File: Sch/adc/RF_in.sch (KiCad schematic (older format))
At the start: 48 parts, among them J3 JP2, J4 JP2, U1 LTC2292, U2 BGA2818, U3 TLV711, X1 ECS-TXO-2520

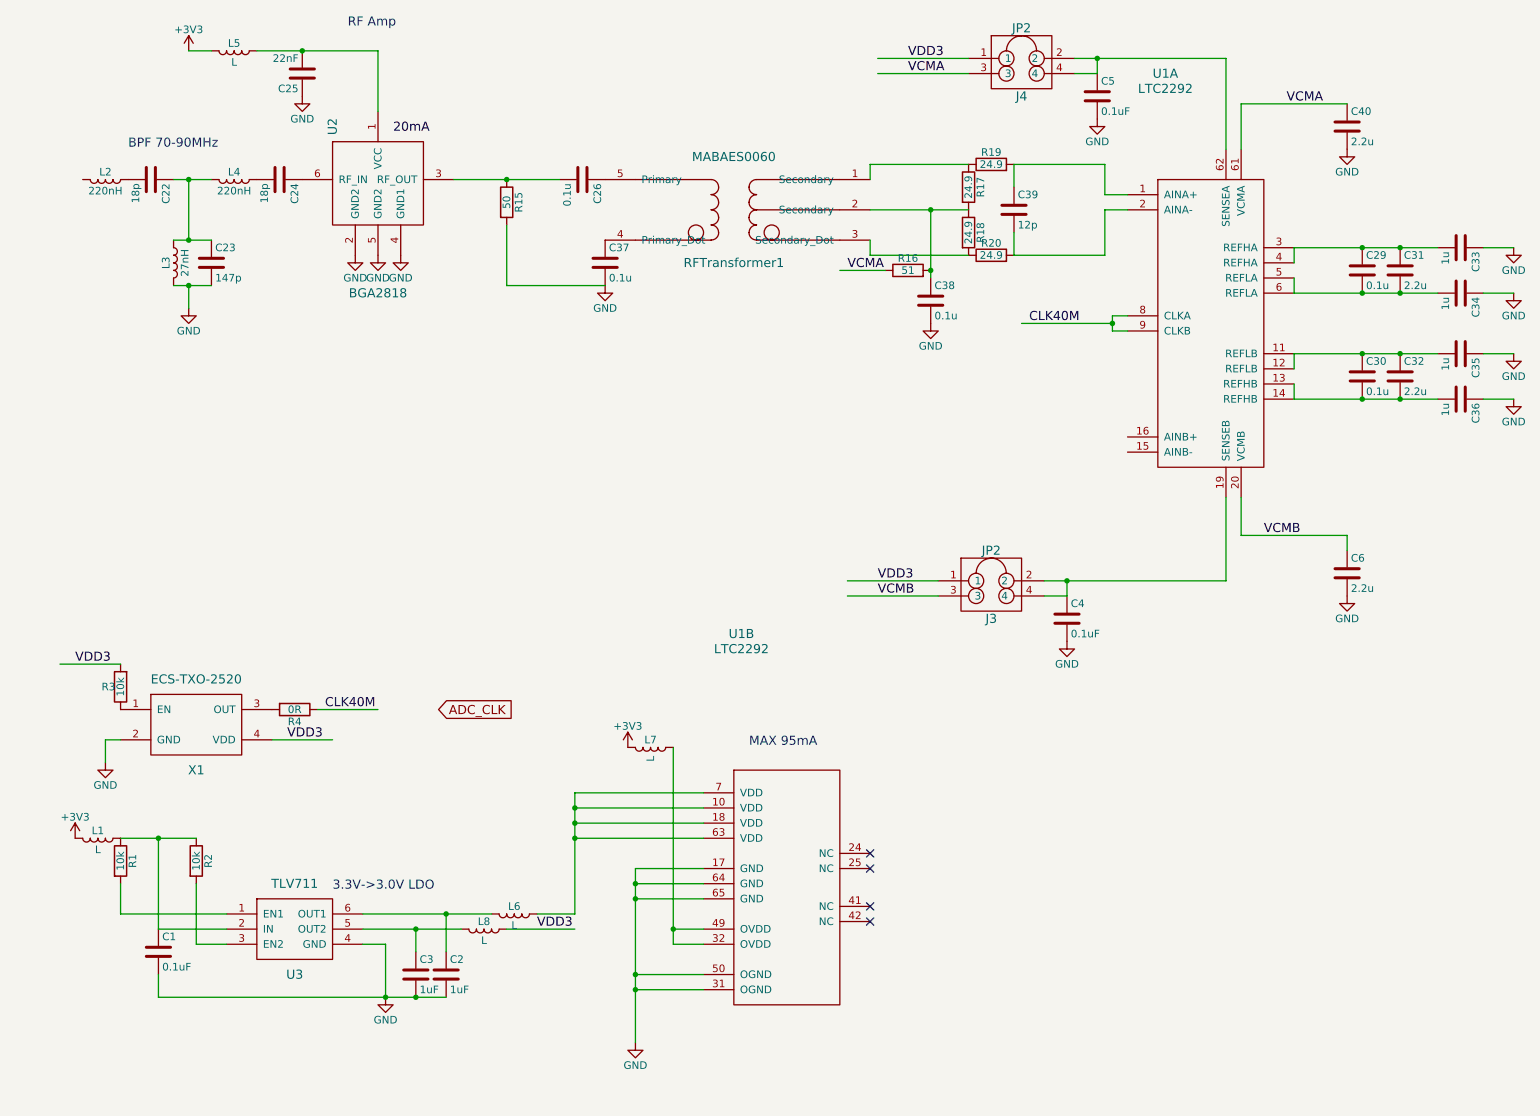
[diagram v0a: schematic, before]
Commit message: Add B-ch of the ADC
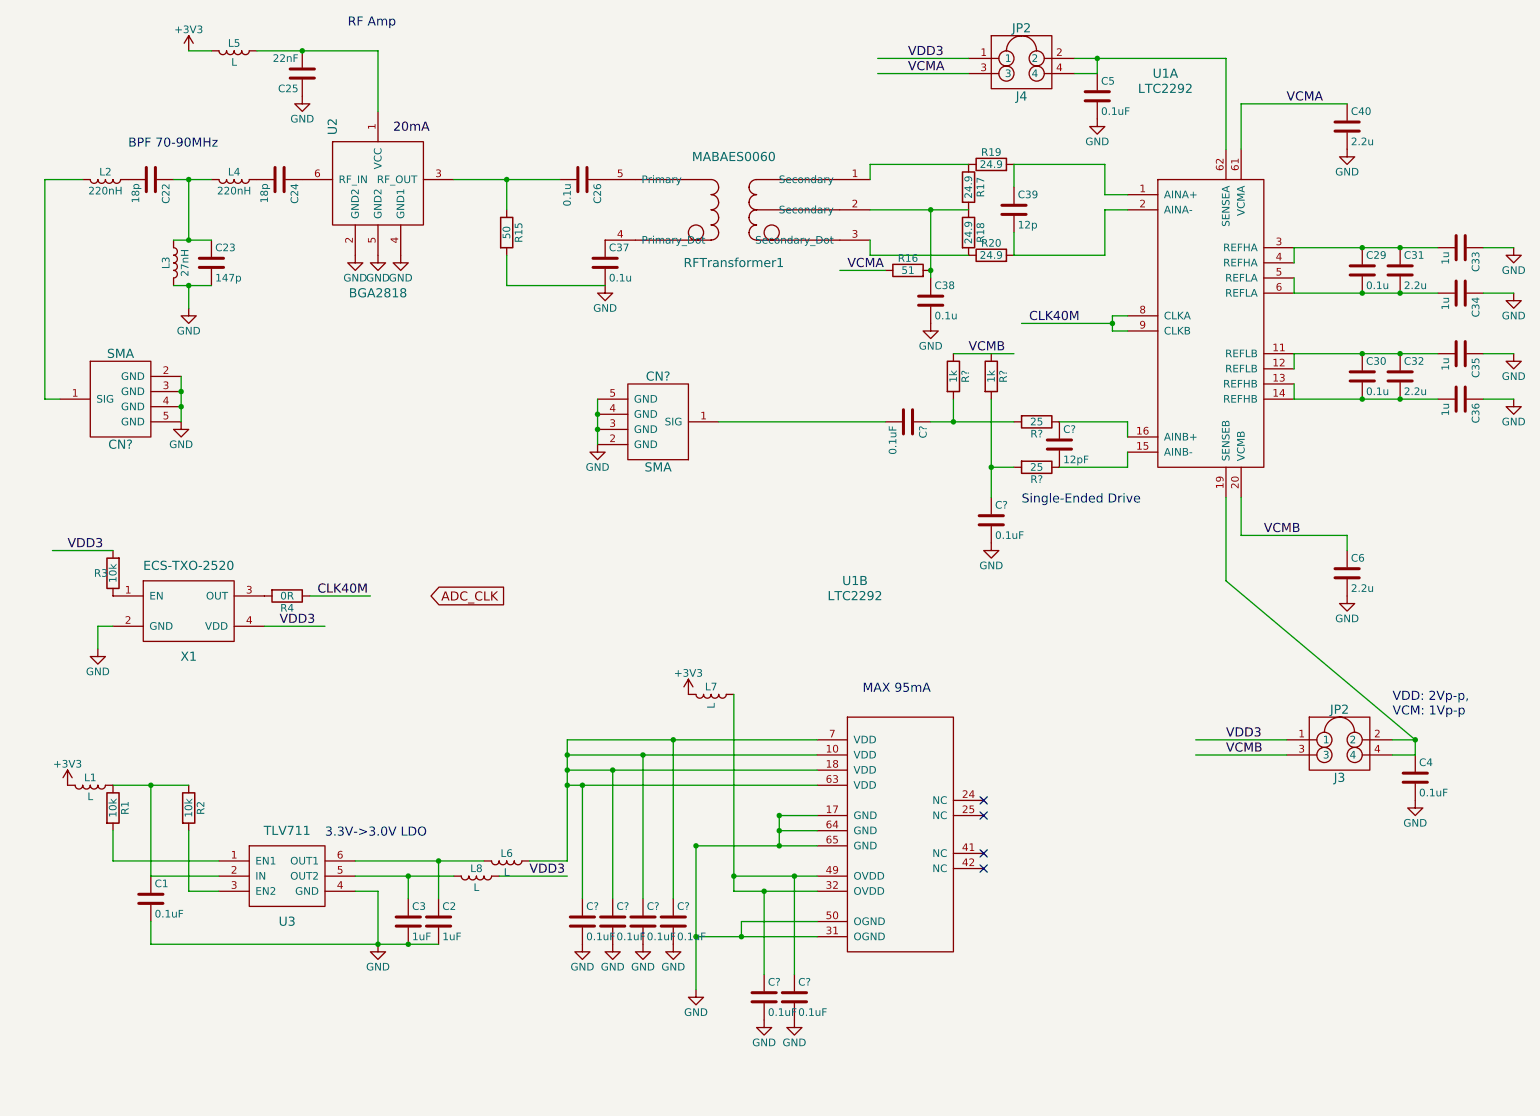
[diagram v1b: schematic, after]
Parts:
- added C? (x8): 0.1uF, symbol C
- added C?: 12pF, symbol C
- added CN? (x2): SMA, symbol SMA
- added R? (x2): 25, symbol R
- added R? (x2): 1k, symbol R
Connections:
- wire segments 95 -> 120
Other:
- note added: "Single-Ended Drive"
- note added: "VDD: 2Vp-p,\nVCM: 1Vp-p"
- moved on the sheet: C1, C2, C3, C4, J3, L1, L6, L7, L8, R1, R15, R2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

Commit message: Almost finished except Audio
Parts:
- added C12: 22nF, symbol C
- added C18, C20, C9: 0.1uF, symbol C
- added C19: 1uF, symbol C
- added J5: JP2, symbol JP2
- added L10, L9: L, symbol L
- added R9: 10k, symbol R
- added U4: BGA2818, symbol BGA2818
- added U5: CDCLVC1102, symbol CDCLVC1102
- R15: value 50 -> DNL
- R4: value 0R -> 50
- gave numbers to parts that had none: 15
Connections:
- net labels added: AMP_OUT, VCC
- wire segments 120 -> 140
- no-connect marks 4 -> 6
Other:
- note added: "max 6mA"
- moved on the sheet: C1, C10, C11, C13, C14, C2, C3, C7, C8, CN2, L1, L6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

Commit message: Fix MODE pin voltage of the ADC
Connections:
- wire segments 140 -> 142
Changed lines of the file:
@@
 $EndComp
 $Comp
-L GND #PWR013
+L GND #PWR012
 U 1 1 58A1C19C
 P 3100 2100
-F 0 "#PWR013" H 3100 1850 50  0001 C CNN
+F 0 "#PWR012" H 3100 1850 50  0001 C CNN
 F 1 "GND" H 3100 1950 50  0000 C CNN
 F 2 "" H 3100 2100 50  0000 C CNN
@@
 $EndComp
 $Comp
-L GND #PWR014
+L GND #PWR013
 U 1 1 58A1C1B6
 P 2950 2100
-F 0 "#PWR014" H 2950 1850 50  0001 C CNN
+F 0 "#PWR013" H 2950 1850 50  0001 C CNN
 F 1 "GND" H 2950 1950 50  0000 C CNN
 F 2 "" H 2950 2100 50  0000 C CNN
@@
 $EndComp
 $Comp
-L GND #PWR015
+L GND #PWR014
 U 1 1 58A1C1C7
 P 2800 2100
-F 0 "#PWR015" H 2800 1850 50  0001 C CNN
+F 0 "#PWR014" H 2800 1850 50  0001 C CNN
 F 1 "GND" H 2800 1950 50  0000 C CNN
 F 2 "" H 2800 2100 50  0000 C CNN
@@
 $EndComp
 $Comp
-L GND #PWR016
+L GND #PWR015
 U 1 1 58A1C6CA
 P 2450 1050
-F 0 "#PWR016" H 2450 800 50  0001 C CNN
+F 0 "#PWR015" H 2450 800 50  0001 C CNN
 F 1 "GND" H 2450 900 50  0000 C CNN
 F 2 "" H 2450 1050 50  0000 C CNN
@@
 $EndComp
 $Comp
-L +3V3 #PWR017
+L +3V3 #PWR016
 U 1 1 58A1C6DD
 P 1700 750
-F 0 "#PWR017" H 1700 600 50  0001 C CNN
+F 0 "#PWR016" H 1700 600 50  0001 C CNN
 F 1 "+3V3" H 1700 890 50  0000 C CNN
 F 2 "" H 1700 750 50  0000 C CNN
@@
 $EndComp
 $Comp
-L GND #PWR018
+L GND #PWR017
 U 1 1 58A1CD2C
 P 1700 2450
-F 0 "#PWR018" H 1700 2200 50  0001 C CNN
+F 0 "#PWR017" H 1700 2200 50  0001 C CNN
 F 1 "GND" H 1700 2300 50  0000 C CNN
 F 2 "" H 1700 2450 50  0000 C CNN
@@
 $EndComp
 $Comp
-L +3V3 #PWR019
+L +3V3 #PWR018
 U 1 1 58A443A9
 P 4750 5350
-F 0 "#PWR019" H 4750 5200 50  0001 C CNN
+F 0 "#PWR018" H 4750 5200 50  0001 C CNN
 F 1 "+3V3" H 4750 5490 50  0000 C CNN
 F 2 "" H 4750 5350 50  0000 C CNN
@@
 $EndComp
 $Comp
-L GND #PWR020
+L GND #PWR019
 U 1 1 58A44759
 P 4800 7300
-F 0 "#PWR020" H 4800 7050 50  0001 C CNN
+F 0 "#PWR019" H 4800 7050 50  0001 C CNN
 F 1 "GND" H 4800 7150 50  0000 C CNN
 F 2 "" H 4800 7300 50  0000 C CNN
@@
 $EndComp
 $Comp
-L GND #PWR021
+L GND #PWR020
 U 1 1 58A3A665
 P 10450 2050
-F 0 "#PWR021" H 10450 1800 50  0001 C CNN
+F 0 "#PWR020" H 10450 1800 50  0001 C CNN
 F 1 "GND" H 10450 1900 50  0000 C CNN
 F 2 "" H 10450 2050 50  0000 C CNN
@@
 $EndComp
 $Comp
-L GND #PWR022
+L GND #PWR021
 U 1 1 58A3A6A7
 P 10450 2350
-F 0 "#PWR022" H 10450 2100 50  0001 C CNN
+F 0 "#PWR021" H 10450 2100 50  0001 C CNN
 F 1 "GND" H 10450 2200 50  0000 C CNN
 F 2 "" H 10450 2350 50  0000 C CNN
@@
 $EndComp
 $Comp
-L GND #PWR023
+L GND #PWR022
 U 1 1 58A3B003
 P 10450 2750
-F 0 "#PWR023" H 10450 2500 50  0001 C CNN
+F 0 "#PWR022" H 10450 2500 50  0001 C CNN
 F 1 "GND" H 10450 2600 50  0000 C CNN
 F 2 "" H 10450 2750 50  0000 C CNN
@@
 $EndComp
 $Comp
-L GND #PWR024
+L GND #PWR023
 U 1 1 58A3B009
 P 10450 3050
-F 0 "#PWR024" H 10450 2800 50  0001 C CNN
+F 0 "#PWR023" H 10450 2800 50  0001 C CNN
 F 1 "GND" H 10450 2900 50  0000 C CNN
 F 2 "" H 10450 3050 50  0000 C CNN
@@
 $EndComp
 $Comp
-L GND #PWR025
+L GND #PWR024
 U 1 1 58A3CC08
 P 6600 2550
-F 0 "#PWR025" H 6600 2300 50  0001 C CNN
+F 0 "#PWR024" H 6600 2300 50  0001 C CNN
 F 1 "GND" H 6600 2400 50  0000 C CNN
 F 2 "" H 6600 2550 50  0000 C CNN
@@
 VCMA
 $Comp
-L GND #PWR026
+L GND #PWR025
 U 1 1 58A3D81B
 P 9350 1400
-F 0 "#PWR026" H 9350 1150 50  0001 C CNN
+F 0 "#PWR025" H 9350 1150 50  0001 C CNN
 F 1 "GND" H 9350 1250 50  0000 C CNN
 F 2 "" H 9350 1400 50  0000 C CNN
@@
 $EndComp
 $Comp
-L GND #PWR027
+L GND #PWR026
 U 1 1 58A3F653
 P 4450 2300
-F 0 "#PWR027" H 4450 2050 50  0001 C CNN
+F 0 "#PWR026" H 4450 2050 50  0001 C CNN
 F 1 "GND" H 4450 2150 50  0000 C CNN
 F 2 "" H 4450 2300 50  0000 C CNN
@@
 $EndComp
 $Comp
-L +3V3 #PWR028
+L +3V3 #PWR027
 U 1 1 58A5E201
 P 650 5950
-F 0 "#PWR028" H 650 5800 50  0001 C CNN
+F 0 "#PWR027" H 650 5800 50  0001 C CNN
 F 1 "+3V3" H 650 6090 50  0000 C CNN
 F 2 "" H 650 5950 50  0000 C CNN
@@
 $EndComp
 $Comp
-L GND #PWR029
+L GND #PWR028
 U 1 1 58A5EF6D
 P 2700 7000
-F 0 "#PWR029" H 2700 6750 50  0001 C CNN
+F 0 "#PWR028" H 2700 6750 50  0001 C CNN
 F 1 "GND" H 2700 6850 50  0000 C CNN
 F 2 "" H 2700 7000 50  0000 C CNN
@@
 $EndComp
 $Comp
-L GND #PWR030
+L GND #PWR029
 U 1 1 58A651BF
 P 1050 5100
-F 0 "#PWR030" H 1050 4850 50  0001 C CNN
+F 0 "#PWR029" H 1050 4850 50  0001 C CNN
 F 1 "GND" H 1050 4950 50  0000 C CNN
 F 2 "" H 1050 5100 50  0000 C CNN
@@
 $EndComp
 $Comp
-L GND #PWR031
+L GND #PWR030
 U 1 1 58A6B351
 P 7700 1200
-F 0 "#PWR031" H 7700 950 50  0001 C CNN
+F 0 "#PWR030" H 7700 950 50  0001 C CNN
 F 1 "GND" H 7700 1050 50  0000 C CNN
 F 2 "" H 7700 1200 50  0000 C CNN
@@
 VCMA
 $Comp
-L GND #PWR032
+L GND #PWR031
 U 1 1 58A6C57D
 P 9350 4350
-F 0 "#PWR032" H 9350 4100 50  0001 C CNN
+F 0 "#PWR031" H 9350 4100 50  0001 C CNN
 F 1 "GND" H 9350 4200 50  0000 C CNN
 F 2 "" H 9350 4350 50  0000 C CNN
@@
 $EndComp
 $Comp
-L GND #PWR033
+L GND #PWR032
 U 1 1 58A6CD2B
 P 9800 5700
-F 0 "#PWR033" H 9800 5450 50  0001 C CNN
+F 0 "#PWR032" H 9800 5450 50  0001 C CNN
 F 1 "GND" H 9800 5550 50  0000 C CNN
 F 2 "" H 9800 5700 50  0000 C CNN
@@
 ADC_CLK
 $Comp
-L GND #PWR034
+L GND #PWR033
 U 1 1 58A70E23
 P 4050 7000
-F 0 "#PWR034" H 4050 6750 50  0001 C CNN
+F 0 "#PWR033" H 4050 6750 50  0001 C CNN
 F 1 "GND" H 4050 6850 50  0000 C CNN
 F 2 "" H 4050 7000 50  0000 C CNN
@@
 $EndComp
 $Comp
-L GND #PWR035
+L GND #PWR034
 U 1 1 58A70EA4
 P 4250 7000
-F 0 "#PWR035" H 4250 6750 50  0001 C CNN
+F 0 "#PWR034" H 4250 6750 50  0001 C CNN
 F 1 "GND" H 4250 6850 50  0000 C CNN
 F 2 "" H 4250 7000 50  0000 C CNN
@@
 $EndComp
 $Comp
-L GND #PWR036
+L GND #PWR035
 U 1 1 58A70F2D
 P 4450 7000
-F 0 "#PWR036" H 4450 6750 50  0001 C CNN
+F 0 "#PWR035" H 4450 6750 50  0001 C CNN
 F 1 "GND" H 4450 6850 50  0000 C CNN
 F 2 "" H 4450 7000 50  0000 C CNN
@@
 $EndComp
 $Comp
-L GND #PWR037
+L GND #PWR036
 U 1 1 58A70FB2
 P 4650 7000
-F 0 "#PWR037" H 4650 6750 50  0001 C CNN
+F 0 "#PWR036" H 4650 6750 50  0001 C CNN
 F 1 "GND" H 4650 6850 50  0000 C CNN
 F 2 "" H 4650 7000 50  0000 C CNN
@@
 $EndComp
 $Comp
-L GND #PWR038
+L GND #PWR037
 U 1 1 58A72283
 P 5250 7500
-F 0 "#PWR038" H 5250 7250 50  0001 C CNN
+F 0 "#PWR037" H 5250 7250 50  0001 C CNN
 F 1 "GND" H 5250 7350 50  0000 C CNN
 F 2 "" H 5250 7500 50  0000 C CNN
@@
 $EndComp
 $Comp
-L GND #PWR039
+L GND #PWR038
 U 1 1 58A72318
 P 5450 7500
-F 0 "#PWR039" H 5450 7250 50  0001 C CNN
+F 0 "#PWR038" H 5450 7250 50  0001 C CNN
 F 1 "GND" H 5450 7350 50  0000 C CNN
 F 2 "" H 5450 7500 50  0000 C CNN
@@
 VCMB
 $Comp
-L GND #PWR040
+L GND #PWR039
 U 1 1 58A75DF8
 P 7000 4000
-F 0 "#PWR040" H 7000 3750 50  0001 C CNN
+F 0 "#PWR039" H 7000 3750 50  0001 C CNN
 F 1 "GND" H 7000 3850 50  0000 C CNN
 F 2 "" H 7000 4000 50  0000 C CNN
@@
 $EndComp
 $Comp
-L GND #PWR041
+L GND #PWR040
 U 1 1 58A7AD61
 P 1650 3200
-F 0 "#PWR041" H 1650 2950 50  0001 C CNN
+F 0 "#PWR040" H 1650 2950 50  0001 C CNN
 F 1 "GND" H 1650 3050 50  0000 C CNN
 F 2 "" H 1650 3200 50  0000 C CNN
@@
 $EndComp
 $Comp
-L GND #PWR042
+L GND #PWR041
 U 1 1 58A7B9E1
 P 5200 3700
-F 0 "#PWR042" H 5200 3450 50  0001 C CNN
+F 0 "#PWR041" H 5200 3450 50  0001 C CNN
 F 1 "GND" H 5200 3550 50  0000 C CNN
 F 2 "" H 5200 3700 50  0000 C CNN
@@
 $EndComp
 $Comp
-L GND #PWR043
+L GND #PWR042
 U 1 1 58A83941
 P 5650 2750
-F 0 "#PWR043" H 5650 2500 50  0001 C CNN
+F 0 "#PWR042" H 5650 2500 50  0001 C CNN
 F 1 "GND" H 5650 2600 50  0000 C CNN
 F 2 "" H 5650 2750 50  0000 C CNN
@@
 $EndComp
 $Comp
-L GND #PWR044
+L GND #PWR043
 U 1 1 58A85320
 P 5350 3700
-F 0 "#PWR044" H 5350 3450 50  0001 C CNN
+F 0 "#PWR043" H 5350 3450 50  0001 C CNN
 F 1 "GND" H 5350 3550 50  0000 C CNN
 F 2 "" H 5350 3700 50  0000 C CNN
@@
 $EndComp
 $Comp
-L GND #PWR045
+L GND #PWR044
 U 1 1 58A853F7
 P 5500 3700
-F 0 "#PWR045" H 5500 3450 50  0001 C CNN
+F 0 "#PWR044" H 5500 3450 50  0001 C CNN
 F 1 "GND" H 5500 3550 50  0000 C CNN
 F 2 "" H 5500 3700 50  0000 C CNN
@@
 	2400 4100 3300 4100
 $Comp
-L +3V3 #PWR046
+L +3V3 #PWR045
 U 1 1 58A88C4E
 P 1950 4100
-F 0 "#PWR046" H 1950 3950 50  0001 C CNN
+F 0 "#PWR045" H 1950 3950 50  0001 C CNN
 F 1 "+3V3" H 1950 4240 50  0000 C CNN
 F 2 "" H 1950 4100 50  0000 C CNN
@@
 	2650 4400 2850 4400
 $Comp
-L GND #PWR047
+L GND #PWR046
 U 1 1 58A897F9
 P 2650 4400
-F 0 "#PWR047" H 2650 4150 50  0001 C CNN
+F 0 "#PWR046" H 2650 4150 50  0001 C CNN
 F 1 "GND" H 2650 4250 50  0000 C CNN
 F 2 "" H 2650 4400 50  0000 C CNN
@@
 Connection ~ 1150 4100
 $Comp
-L GND #PWR048
+L GND #PWR047
 U 1 1 58A8B1A7
 P 2250 5250
-F 0 "#PWR048" H 2250 5000 50  0001 C CNN
+F 0 "#PWR047" H 2250 5000 50  0001 C CNN
 F 1 "GND" H 2250 5100 50  0000 C CNN
 F 2 "" H 2250 5250 50  0000 C CNN
@@
 NoConn ~ 3300 5150
 $Comp
-L GND #PWR049
+L GND #PWR048
 U 1 1 58A8C065
 P 3400 5150
-F 0 "#PWR049" H 3400 4900 50  0001 C CNN
+F 0 "#PWR048" H 3400 4900 50  0001 C CNN
 F 1 "GND" H 3400 5000 50  0000 C CNN
 F 2 "" H 3400 5150 50  0000 C CNN
@@
 max 6mA
 $Comp
-L GND #PWR050
+L GND #PWR049
 U 1 1 58A8E85E
 P 3050 3350
-F 0 "#PWR050" H 3050 3100 50  0001 C CNN
+F 0 "#PWR049" H 3050 3100 50  0001 C CNN
 F 1 "GND" H 3050 3200 50  0000 C CNN
 F 2 "" H 3050 3350 50  0000 C CNN
@@
 $EndComp
 Connection ~ 3050 3350
+Text GLabel 3600 7200 0    60   Input ~ 0
+VDD3
+Wire Wire Line
+	3700 6550 3700 7200
+Wire Wire Line
+	3700 7200 3600 7200
+Connection ~ 3700 6550
 $EndSCHEMATC
